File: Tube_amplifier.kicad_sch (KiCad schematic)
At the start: 76 parts, among them J1 AudioJack3, J10 output, J11 Conn_01x03, J12 Conn_01x03, J13 Conn_01x04, J2 Input, J3 Conn_01x04, J4 output, J5 220V, J6 Conn_01x04, J7 Conn_01x04, J8 Indication, J9 output, SW1 SW_Push, T1 Transformer_SP_1S, T2 Transformer_1P_2S, U1 6N2P, U2 6P14P, U3 6H2P, U4 6H2P, U5 6E1P, U6 6E1P

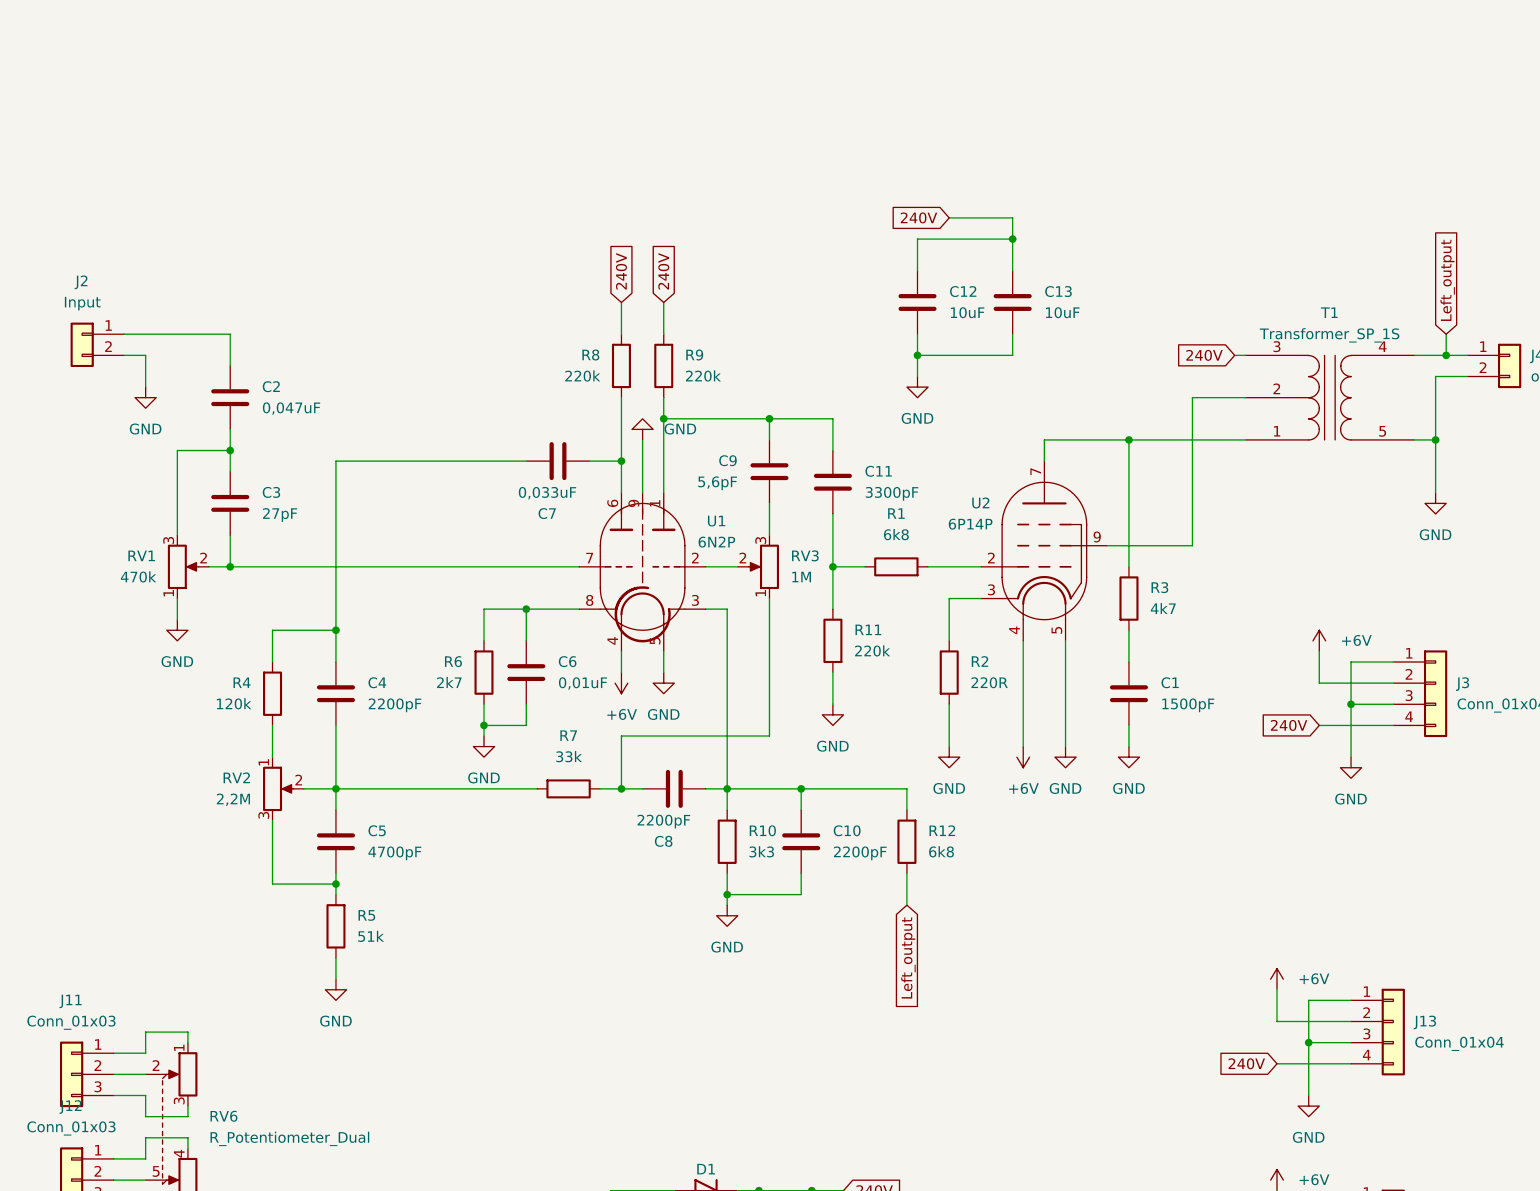
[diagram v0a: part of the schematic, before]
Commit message: New schematic
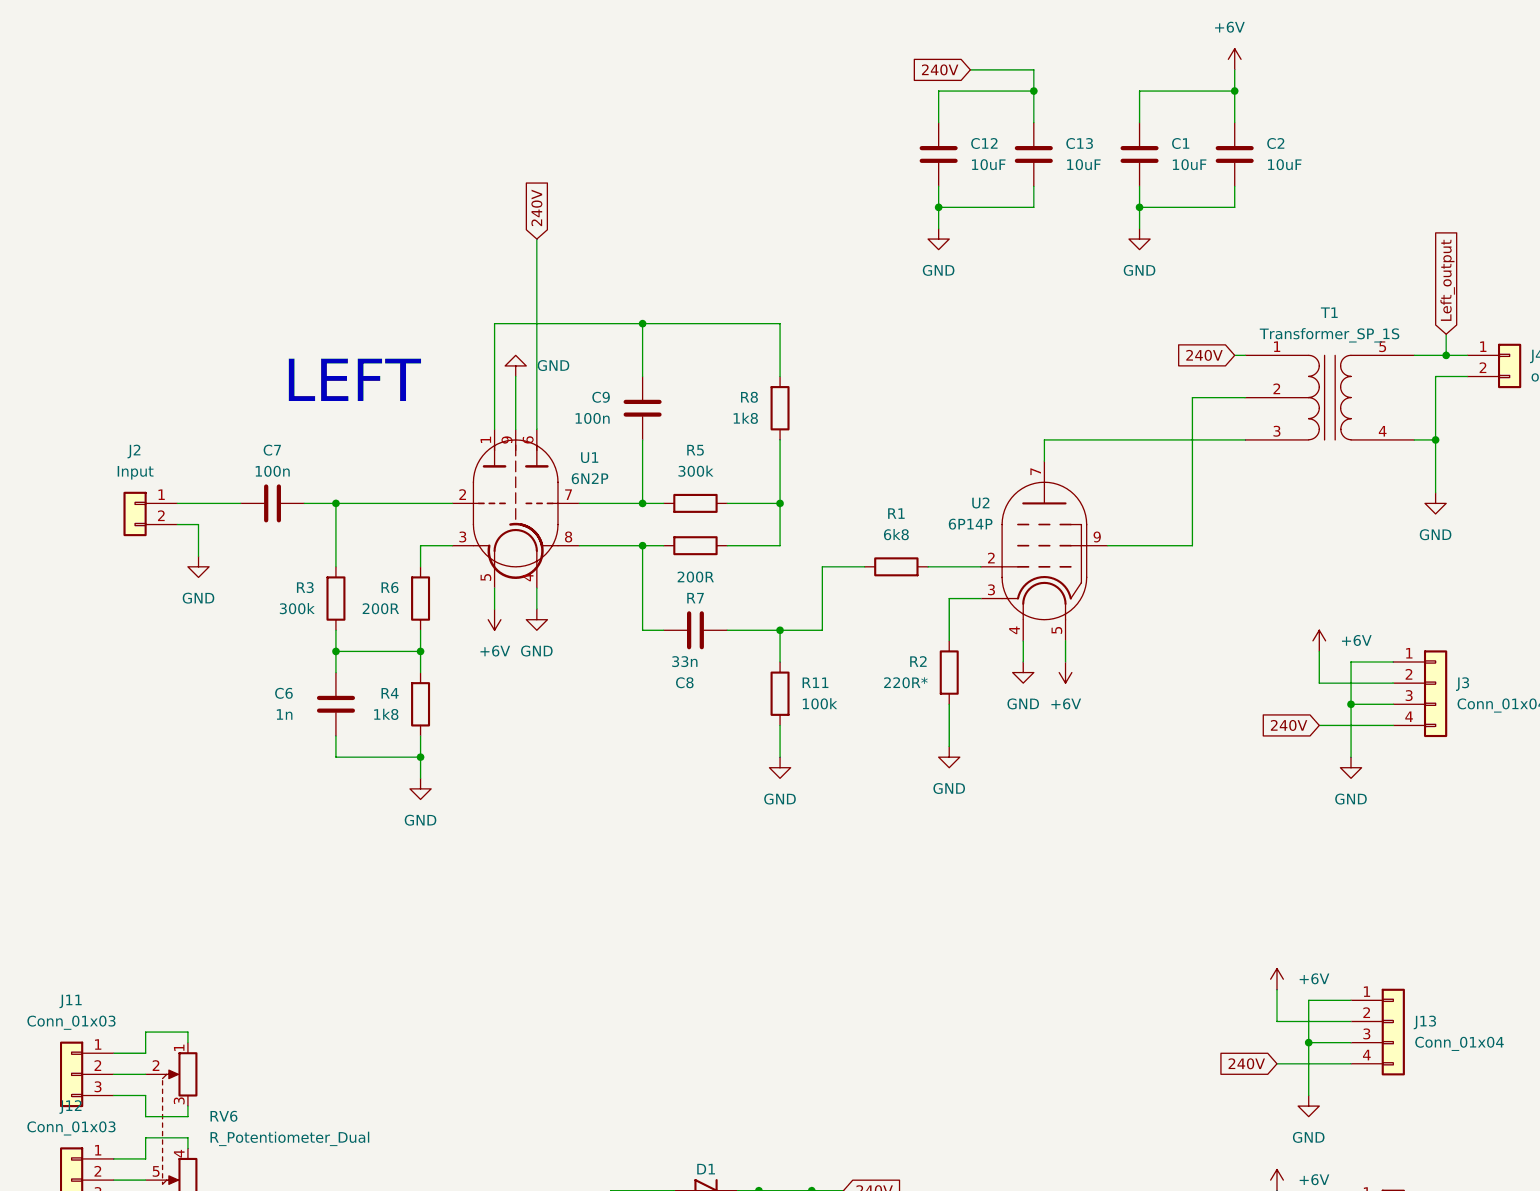
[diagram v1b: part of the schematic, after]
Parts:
- removed C10, C4: 2200pF, spdf1626_lib:C_THT_K73-17_P5.00mm, symbol Device:C
- removed C11: 3300pF, spdf1626_lib:C_THT_K73-17_P5.00mm, symbol Device:C
- removed C3: 27pF, spdf1626_lib:C_THT_K73-17_P5.00mm, symbol Device:C
- removed C5: 4700pF, spdf1626_lib:C_THT_K73-17_P5.00mm, symbol Device:C
- removed R10: 3k3, spdf1626_lib:R_THT_025W, symbol Device:R
- removed R12: 6k8, spdf1626_lib:R_THT_025W, symbol Device:R
- removed R9: 220k, spdf1626_lib:R_THT_025W, symbol Device:R
- removed RV1: 470k, spdf1626_lib:PinHeader_1x03_P2.54mm, symbol Device:R_Potentiometer
- removed RV2: 2,2M, spdf1626_lib:Potentiometer_THT_CA9V, symbol Device:R_Potentiometer
- removed RV3: 1M, spdf1626_lib:Potentiometer_THT_CA9V, symbol Device:R_Potentiometer
- C1: value 1500pF -> 10uF; footprint spdf1626_lib:C_THT_K73-17_P5.00mm -> Capacitor_THT:CP_Radial_D5.0mm_P2.00mm
- C2: value 0,047uF -> 10uF; footprint spdf1626_lib:C_THT_K73-17_P5.00mm -> Capacitor_THT:CP_Radial_D5.0mm_P2.00mm
- C6: value 0,01uF -> 1n
- C7: value 0,033uF -> 100n; footprint spdf1626_lib:C_THT_K73-17_P5.00mm -> spdf1626_lib:C_THT_K73-17_P9.00mm
- C8: value 2200pF -> 33n
- C9: value 5,6pF -> 100n; footprint spdf1626_lib:C_THT_K73-17_P5.00mm -> spdf1626_lib:C_THT_K73-17_P9.00mm
- R11: value 220k -> 100k
- R2: value 220R -> 220R*
- R3: value 4k7 -> 300k; footprint spdf1626_lib:R_THT_1W -> spdf1626_lib:R_THT_025W
- R4: value 120k -> 1k8
- R5: value 51k -> 300k
- R6: value 2k7 -> 200R
- R7: value 33k -> 200R
- R8: value 220k -> 1k8
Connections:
- net +6V: now also C1.1, C2.1, U1.5, U2.5; no longer U1.4, U2.4
- net 240V: now also T1.1 (PR1), U1.6; no longer R8.2, T1.3 (PR2)
- net GND: now also C2.2, R4.1, T1.4 (S1), U1.4, U2.4; no longer R5.1, R6.1, T1.5 (S2), U1.5, U2.5
- net Left_output: now also T1.5 (S2); no longer T1.4 (S1)
- net at J2.1 (Pin_1): now also C7.1; no longer C2.1
- net at R4.2: now also C6.1, R3.1, R6.1; no longer C7.1
- net at U1.7: now also C9.1, R5.2
- net at C8.2: now also R1.1, R11.1; no longer U1.3
- net at R7.1: now also R5.1, R8.1; no longer C8.1
- net at R7.2: now also C8.1, U1.8
- net at R3.2: now also C7.2, U1.2; no longer C1.1
- net at C9.2, U1.1: now also R8.2
- new net: R6.2, U1.3
- new net: T1.3 (PR2), U2.7
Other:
- note added: "LEFT"
- moved on the sheet: C12, C13, C6, C7, C8, C9, J2, R11, R6, U1

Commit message: Curved traces
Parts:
- removed R11: 100k, spdf1626_lib:R_THT_025W, symbol Device:R
- added RV1: 100k, spdf1626_lib:Potentiometer_THT_CA9V, symbol Device:R_Potentiometer
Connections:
- net GND: now also RV1.3
- net at C8.2: now also RV1.1; no longer R1.1
- new net: R1.1, RV1.2
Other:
- note removed: "LEFT"
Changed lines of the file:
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@@
   (junction (at 64.77 66.04) (diameter 0) (color 0 0 0 0)
   )
-  (junction (at 107.95 63.5) (diameter 0) (color 0 0 0 0)
-  )
   (junction (at 251.46 34.29) (diameter 0) (color 0 0 0 0)
   )
@@
     (stroke (width 0) (type default) (color 0 0 0 0))
   )
-  (wire (pts (xy 113.03 63.5) (xy 113.03 55.88))
+  (wire (pts (xy 113.03 55.88) (xy 113.03 71.12))
     (stroke (width 0) (type default) (color 0 0 0 0))
   )
@@
     (stroke (width 0) (type default) (color 0 0 0 0))
   )
-  (wire (pts (xy 107.95 63.5) (xy 113.03 63.5))
-    (stroke (width 0) (type default) (color 0 0 0 0))
-  )
   (wire (pts (xy 240.03 152.4) (xy 242.57 152.4))
     (stroke (width 0) (type default) (color 0 0 0 0))
@@
     (stroke (width 0) (type default) (color 0 0 0 0))
   )
+  (wire (pts (xy 111.76 71.12) (xy 113.03 71.12))
+    (stroke (width 0) (type default) (color 0 0 0 0))
+  )
   (wire (pts (xy 86.36 171.45) (xy 86.36 168.91))
     (stroke (width 0) (type default) (color 0 0 0 0))
@@
   (wire (pts (xy 139.7 154.94) (xy 139.7 156.21))
     (stroke (width 0) (type default) (color 0 0 0 0))
-  )
-  (text "LEFT" (at 48.26 36.83 0)
-    (effects (font (size 5.08 5.08)) (justify left bottom))
   )
   (text "240V" (at 77.47 156.21 0)
@@
     (pin "1")
     (pin "2")
+  )
+  (symbol (lib_id "Device:R_Potentiometer") (at 107.95 71.12 0) (unit 1)
+    (in_bom yes) (on_board yes) (fields_autoplaced)
+    (property "Reference" "RV1" (id 0) (at 105.41 69.8499 0)
+      (effects (font (size 1.27 1.27)) (justify right))
+    )
+    (property "Value" "100k" (id 1) (at 105.41 72.3899 0)
+      (effects (font (size 1.27 1.27)) (justify right))
+    )
+    (property "Footprint" "spdf1626_lib:Potentiometer_THT_CA9V" (id 2) (at 107.95 71.12 0)
+      (effects (font (size 1.27 1.27)) hide)
+    )
+    (property "Datasheet" "~" (id 3) (at 107.95 71.12 0)
+      (effects (font (size 1.27 1.27)) hide)
+    )
+    (pin "1")
+    (pin "2")
+    (pin "3")
   )
   (symbol (lib_id "spdf1626:L_Coupled") (at 31.75 158.75 0) (unit 1)
@@
     (pin "1")
   )
-  (symbol (lib_id "Device:R") (at 107.95 71.12 0) (mirror y) (unit 1)
-    (in_bom yes) (on_board yes) (fields_autoplaced)
-    (property "Reference" "R11" (id 0) (at 110.49 69.8499 0)
-      (effects (font (size 1.27 1.27)) (justify right))
-    )
-    (property "Value" "100k" (id 1) (at 110.49 72.3899 0)
-      (effects (font (size 1.27 1.27)) (justify right))
-    )
-    (property "Footprint" "spdf1626_lib:R_THT_025W" (id 2) (at 109.728 71.12 90)
-      (effects (font (size 1.27 1.27)) hide)
-    )
-    (property "Datasheet" "~" (id 3) (at 107.95 71.12 0)
-      (effects (font (size 1.27 1.27)) hide)
-    )
-    (pin "1")
-    (pin "2")
-  )
   (symbol (lib_id "Connector_Generic:Conn_01x03") (at 22.86 129.54 0) (mirror y) (unit 1)
     (in_bom yes) (on_board yes) (fields_autoplaced)
@@
       (reference "R8") (unit 1) (value "1k8") (footprint "spdf1626_lib:R_THT_025W")
     )
-    (path "/d7dabff1-d3e8-43d3-9166-fdc019d9e19a"
-      (reference "R11") (unit 1) (value "100k") (footprint "spdf1626_lib:R_THT_025W")
-    )
     (path "/ca10b4ec-5423-4d02-a148-7b58fb08b46f"
       (reference "R13") (unit 1) (value "1M") (footprint "spdf1626_lib:R_THT_025W")
@@
       (reference "R17") (unit 1) (value "1M") (footprint "spdf1626_lib:R_THT_025W")
     )
+    (path "/2f680110-9ea0-4f48-b5a6-990648d3cde2"
+      (reference "RV1") (unit 1) (value "100k") (footprint "spdf1626_lib:Potentiometer_THT_CA9V")
+    )
     (path "/74ca2db8-4116-473d-8df0-bbab22bc42c2"

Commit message: High Voltage stabilizer
Create high voltage stabilizer
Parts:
- removed C14: 100uF, Capacitor_THT:CP_Radial_D22.0mm_P10.00mm_SnapIn, symbol Device:C
- removed C15: 100uF_10V, Capacitor_THT:CP_Radial_D6.3mm_P2.50mm, symbol Device:C
- removed C16, C17, C18, C19: 6800pF, spdf1626_lib:C_THT_K73-17_P5.00mm, symbol Device:C
- removed D1, D10, D2, D3, D4, D9: 1n4007, Diode_THT:D_DO-41_SOD81_P12.70mm_Horizontal, symbol Device:D
- removed D5, D6, D7, D8: 10A10, Diode_THT:D_DO-27_P15.24mm_Horizontal, symbol Device:D
- removed J1: AudioJack3, Connector_Audio:Jack_6.35mm_Neutrik_NMJ6HHD2_Horizontal, symbol Connector:AudioJack3
- removed J10, J9: output, spdf1626_lib:PinHeader_1x02_P2.54mm, symbol Connector_Generic:Conn_01x02
- removed J11, J12: Conn_01x03, spdf1626_lib:PinHeader_1x03_P2.54mm, symbol Connector_Generic:Conn_01x03
- removed J13, J6, J7: Conn_01x04, spdf1626_lib:PinHeader_1x04_P2.54mm, symbol Connector_Generic:Conn_01x04
- removed J5: 220V, Connector_Phoenix_MC_HighVoltage:PhoenixContact_MCV_1,5_2-G-5.08_1x02_P5.08mm_Vertical, symbol Connector_Generic:Conn_01x02
- removed J8: Indication, spdf1626_lib:PinHeader_1x03_P2.54mm, symbol Connector_Generic:Conn_01x03
- removed L1: L_Coupled, spdf1626_lib:L_THT_PLA10, symbol spdf1626:L_Coupled
- removed NE1: Lamp_Neon, spdf1626_lib:PinHeader_1x02_P2.54mm, symbol Device:Lamp_Neon
- removed R13, R14, R15, R16, R17: 1M, spdf1626_lib:R_THT_025W, symbol Device:R
- removed RV4, RV5: 470k, spdf1626_lib:Potentiometer_THT_CA9V, symbol Device:R_Potentiometer
- removed RV6: R_Potentiometer_Dual, Potentiometer_THT:Potentiometer_Alps_RK163_Dual_Horizontal, symbol Device:R_Potentiometer_Dual
- removed SW1: SW_Push, Button_Switch_THT:SW_Push_1P2T_Vertical_E-Switch_800UDP8P1A1M6, symbol Switch:SW_Push
- removed T2: Transformer_1P_2S, symbol Device:Transformer_1P_2S
- removed U3, U4: 6H2P, spdf1626_lib:7-pin_tube_socket, symbol spdf1626:6H2P
- removed U5, U6: 6E1P, spdf1626_lib:9-pin_tube_socket, symbol spdf1626:6E1P
- added C3: 33n opt, Capacitor_THT:C_Rect_L7.2mm_W3.0mm_P5.00mm_FKS2_FKP2_MKS2_MKP2, symbol Device:C
- added C? (x4): 6800pF, spdf1626_lib:C_THT_K73-17_P5.00mm, symbol Device:C
- added C? (x5): 100n, spdf1626_lib:C_THT_K73-17_P9.00mm, symbol Device:C
- added C?: 100uF, Capacitor_THT:CP_Radial_D22.0mm_P10.00mm_SnapIn, symbol Device:C
- added C? (x3): 10uF, spdf1626_lib:C_THT_D10.0mm_P5.00mm, symbol Device:C
- added C?: 3300uF_10V, Capacitor_THT:CP_Radial_D6.3mm_P2.50mm, symbol Device:C
- added D? (x7): 1n4007, Diode_THT:D_DO-41_SOD81_P12.70mm_Horizontal, symbol Device:D
- added D? (x4): 1N5821, Diode_THT:D_DO-27_P15.24mm_Horizontal, symbol Device:D
- added J? (x4): Conn_01x04, spdf1626_lib:PinHeader_1x04_P2.54mm, symbol Connector_Generic:Conn_01x04
- added J? (x2): output, spdf1626_lib:PinHeader_1x02_P2.54mm, symbol Connector_Generic:Conn_01x02
- added J? (x2): Conn_01x03, spdf1626_lib:PinHeader_1x03_P2.54mm, symbol Connector_Generic:Conn_01x03
- added J?: Indication, spdf1626_lib:PinHeader_1x03_P2.54mm, symbol Connector_Generic:Conn_01x03
- added J?: 220V, Connector_Phoenix_MC_HighVoltage:PhoenixContact_MCV_1,5_2-G-5.08_1x02_P5.08mm_Vertical, symbol Connector_Generic:Conn_01x02
- added J?: HV_Transformer, spdf1626_lib:PinHeader_1x02_P2.54mm, symbol Connector_Generic:Conn_01x02
- added J?: LV_Transformer, spdf1626_lib:PinHeader_1x02_P2.54mm, symbol Connector_Generic:Conn_01x02
- added J?: Thyratrone, spdf1626_lib:PinHeader_1x03_P2.54mm, symbol Connector_Generic:Conn_01x03
- added J?: Transformers, spdf1626_lib:PinHeader_1x02_P2.54mm, symbol Connector_Generic:Conn_01x02
- added J?: AudioJack3, Connector_Audio:Jack_6.35mm_Neutrik_NMJ6HHD2_Horizontal, symbol Connector:AudioJack3
- added J?: Anodes_enable, Connector_Phoenix_MC_HighVoltage:PhoenixContact_MCV_1,5_2-G-5.08_1x02_P5.08mm_Vertical, symbol Connector_Generic:Conn_01x02
- added K?: SANYOU_SRD_Form_C, Relay_THT:Relay_SPDT_SANYOU_SRD_Series_Form_C, symbol Relay:SANYOU_SRD_Form_C
- added L?: L_Coupled, spdf1626_lib:L_THT_PLA10, symbol spdf1626:L_Coupled
- added NE?: Lamp_Neon, spdf1626_lib:PinHeader_1x02_P2.54mm, symbol Device:Lamp_Neon
- added NE?: Anodes_OK, spdf1626_lib:PinHeader_1x02_P2.54mm, symbol Device:Lamp_Neon
- added Q? (x4): MPSA42, Package_TO_SOT_THT:TO-92_Inline, symbol Transistor_BJT:MPSA42
- added Q?: 2N3904, Package_TO_SOT_THT:TO-92_Inline, symbol Transistor_BJT:2N3904
- added Q?: MJE13003, Package_TO_SOT_THT:TO-126-3_Vertical, symbol Transistor_BJT:MJE13003
- added R12: 680R, spdf1626_lib:R_THT_025W, symbol Device:R
- added R9: 220k opt, spdf1626_lib:R_THT_025W, symbol Device:R
- added R?: 40k, spdf1626_lib:R_THT_025W, symbol Device:R
- added R?: 10k, spdf1626_lib:R_THT_025W, symbol Device:R
- added R?: 50k, spdf1626_lib:R_THT_025W, symbol Device:R
- added R? (x7): 1M, spdf1626_lib:R_THT_025W, symbol Device:R
- added R?: 13k, spdf1626_lib:R_THT_025W, symbol Device:R
- added R? (x2): 100k, spdf1626_lib:R_THT_025W, symbol Device:R
- added R?: 100R, spdf1626_lib:R_THT_1W, symbol Device:R
- added R?: 600R, spdf1626_lib:R_THT_025W, symbol Device:R
- added RV? (x2): 470k, spdf1626_lib:Potentiometer_THT_CA9V, symbol Device:R_Potentiometer
- added RV?: R_Potentiometer_Dual, Potentiometer_THT:Potentiometer_Alps_RK163_Dual_Horizontal, symbol Device:R_Potentiometer_Dual
- added RV?: 10k, spdf1626_lib:Potentiometer_THT_CA9V, symbol Device:R_Potentiometer
- added U?: SG2P, spdf1626_lib:7-pin_tube_socket, symbol spdf1626:SG2P
- added U? (x2): 6E1P, spdf1626_lib:9-pin_tube_socket, symbol spdf1626:6E1P
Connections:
- net +6V: now also C?.1, C?.2, D?.1 (K), D?.1 (K), D?.1 (K), J?.2 (Pin_2), J?.2 (Pin_2), J?.2 (Pin_2), J?.2 (Pin_2), K?.5, U?.5, U?.5
- net 240V: now also J?.1 (Pin_1), J?.4 (Pin_4), J?.4 (Pin_4), J?.4 (Pin_4), J?.4 (Pin_4), R12.2, R9.2, R?.1, R?.1, U?.9, U?.9; no longer C12.1, U1.6
- net GND: now also C?.1, C?.1, C?.1, C?.2, C?.2, C?.2, C?.2, C?.2, C?.2, D?.1 (K), D?.1 (K), D?.2 (A), D?.2 (A), D?.2 (A), D?.2 (A), J?.1 (Pin_1), J?.1 (Pin_1), J?.1 (Pin_1), J?.1 (Pin_1), J?.2 (Pin_2), J?.2 (Pin_2), J?.2 (Pin_2), J?.3 (Pin_3), J?.3 (Pin_3), J?.3 (Pin_3), J?.3 (Pin_3), J?.T, NE?.1, Q?.1 (E), R?.2, RV?.1, RV?.3, U?.2, U?.2, U?.4, U?.4, U?.4
- net at C8.2, RV1.1: now also C3.2
- net at C9.2, R8.2, U1.1: now also C3.1, R9.1
- new net: C?.2, RV?.1
- new net: D?.2 (A), R?.1, RV?.2 (x2)
- new net: R?.1, RV?.3
- new net: J?.1 (Pin_1), J?.R
- new net: Q?.2 (B), Q?.3 (C), R?.1
- new net: C?.1, C?.1, C?.2, J?.2 (Pin_2), Q?.3 (E), R?.1, R?.2
- new net: R?.2, RV?.1
- new net: C?.1, J?.2 (Pin_2), R?.1
- new net: J?.1 (Pin_1), RV?.1
- new net: J?.2 (Pin_2), RV?.2
- new net: J?.3 (Pin_3), RV?.3
- new net: C?.2, RV?.3
- new net: C12.1, R12.1, U1.6
- new net: R?.2, U?.7 (x2)
- new net: J?.1 (Pin_1), RV?.4
- new net: J?.2 (Pin_2), RV?.5
- new net: J?.3 (Pin_3), RV?.6
- new net: Q?.1 (E), Q?.2 (B), Q?.3 (C), R?.1
- new net: Q?.1 (E), Q?.2 (B), R?.2
- new net: C?.1, R?.2, U?.1 (x2)
- new net: D?.1 (K), D?.1 (K), R?.1
- new net: D?.1 (K), D?.2 (A), J?.1 (Pin_1) (x2)
- new net: D?.1 (K), D?.2 (A), J?.2 (Pin_2) (x2)
- new net: C?.2, C?.2, Q?.1 (E), R?.2, U?.1
- new net: C?.1, R?.1, RV?.2
- new net: J?.3 (Pin_3), R?.1
- new net: Q?.2 (B), R?.2 (x2)
- new net: C?.1, J?.1 (Pin_1)
- new net: C?.1, J?.3 (Pin_3)
- new net: D?.2 (A), K?.2, Q?.3 (C)
- new net: J?.1 (Pin_1), J?.S
- new net: NE?.2, R?.1
- new net: J?.1 (Pin_1), L?.1
- new net: J?.2 (Pin_2), L?.4
- new net: Q?.1 (B), Q?.1 (E)
- new net: NE?.1, R?.2
- new net: C?.2, J?.1 (Pin_1), L?.2, NE?.2
- new net: C?.1, J?.2 (Pin_2), L?.3, R?.1
- new net HV: C?.1, C?.2, J?.1 (Pin_1), K?.1, R?.2, R?.2
- new net K1.1: K?.3, Q?.2 (C), Q?.3 (C), Q?.3 (C), R?.1, R?.2
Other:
- moved on the sheet: C1, C12, C13, C2, C6, C7, C8, C9, J2, J3, J4, R1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
